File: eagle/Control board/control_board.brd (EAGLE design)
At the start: 100 x 100 mm, 179 parts, among them SW1 SPST_TACT-EVQQ2, SW2 SPST_TACT-EVQQ2, U1 TCA9554A, U2 LM317, U3 LM317, U4 STM32F446, U5 TCA9554A, U6 TCA9554A, X1 JST-XH-02-PIN-LONG-PAD, X10 JST-XH-07-PIN-LONG-PAD, X11 JST-XH-07-PIN-LONG-PAD, X12 JST-XH-02-PIN-LONG-PAD, X13 JST-XH-03-PIN-LONG-PAD, X14 JST-XH-03-PIN-LONG-PAD, X15 JST-XH-08-PIN-LONG-PAD, X16 JST-XH-02-PIN-LONG-PAD, X17 JST-XH-08-PIN-LONG-PAD, X18 JST-XH-02-PIN-LONG-PAD, X2 JST-XH-06-PIN-LONG-PAD, X3 JST-XH-06-PIN-LONG-PAD, X4 JST-XH-06-PIN-LONG-PAD, X5 JST-XH-06-PIN-LONG-PAD, X6 JST-XH-06-PIN-LONG-PAD, X7 JST-XH-06-PIN-LONG-PAD, X8 JST-XH-04-PIN-LONG-PAD, X9 JST-XH-07-PIN-LONG-PAD

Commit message: Nearly done assigning gpio
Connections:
- removed net N$4: SB43.P$1
- removed net N$43: SB42.P$2
- net M1_2: now also SB19.P$1
- net M1_4: now also SB45.P$1
- net M3_1: no longer SB46.P$2
- net M3_3: no longer SB44.P$2
- net RF4_G: now also SB12.P$1; no longer SB1.P$1
- net RF5_G: now also SB13.P$1; no longer SB36.P$2
- net SW1: now also SB50.P$2
- net SW2: now also SB49.P$2
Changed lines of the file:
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@@
 <signal name="RF4_G">
 <contactref element="SB72" pad="P$1"/>
-<contactref element="SB1" pad="P$1"/>
-<wire x1="27.051" y1="36.576" x2="36.195" y2="44.45" width="0" layer="19" extent="1-1"/>
+<contactref element="SB12" pad="P$1"/>
+<wire x1="36.195" y1="44.45" x2="86.995" y2="54.356" width="0" layer="19" extent="1-1"/>
 </signal>
 <signal name="RF5_G">
 <contactref element="SB77" pad="P$1"/>
-<contactref element="SB36" pad="P$2"/>
-<wire x1="27.051" y1="67.056" x2="36.195" y2="55.88" width="0" layer="19" extent="1-1"/>
+<contactref element="SB13" pad="P$1"/>
+<wire x1="36.195" y1="55.88" x2="86.995" y2="56.896" width="0" layer="19" extent="1-1"/>
 </signal>
 <signal name="RF5_X">
@@
 <signal name="M1_4">
 <contactref element="SB88" pad="P$1"/>
+<contactref element="SB45" pad="P$1"/>
+<wire x1="57.15" y1="18.415" x2="66.929" y2="46.736" width="0" layer="19" extent="1-1"/>
 </signal>
 <signal name="M1_1">
@@
 <signal name="M1_2">
 <contactref element="SB86" pad="P$1"/>
+<contactref element="SB19" pad="P$1"/>
+<wire x1="57.15" y1="13.335" x2="86.995" y2="44.196" width="0" layer="19" extent="1-1"/>
 </signal>
 <signal name="M1_3">
@@
 <signal name="M3_1">
 <contactref element="SB90" pad="P$1"/>
-<contactref element="SB46" pad="P$2"/>
 <contactref element="SB7" pad="P$1"/>
-<wire x1="66.929" y1="54.356" x2="86.995" y2="67.056" width="0" layer="19" extent="1-1"/>
 <wire x1="81.28" y1="10.795" x2="66.929" y2="54.356" width="0" layer="19" extent="1-1"/>
 </signal>
@@
 <signal name="M3_3">
 <contactref element="SB92" pad="P$1"/>
-<contactref element="SB44" pad="P$2"/>
 <contactref element="SB8" pad="P$1"/>
-<wire x1="66.929" y1="51.816" x2="86.995" y2="69.596" width="0" layer="19" extent="1-1"/>
 <wire x1="81.28" y1="15.875" x2="66.929" y2="51.816" width="0" layer="19" extent="1-1"/>
 </signal>
@@
 <wire x1="32.385" y1="85.305" x2="32.385" y2="89.535" width="0.3048" layer="1"/>
 <wire x1="34.925" y1="85.305" x2="32.385" y2="85.305" width="0.3048" layer="1"/>
+<contactref element="SB50" pad="P$2"/>
+<wire x1="4.953" y1="26.416" x2="32.385" y2="85.305" width="0" layer="19" extent="1-1"/>
 </signal>
 <signal name="IMU_VCC">
@@
 <contactref element="X8" pad="1"/>
 <wire x1="43.815" y1="73.025" x2="43.815" y2="77.47" width="0.3048" layer="1"/>
-</signal>
-<signal name="N$43">
-<contactref element="SB42" pad="P$2"/>
 </signal>
 <signal name="SW2">
@@
 <wire x1="42.545" y1="89.535" x2="42.545" y2="85.305" width="0.3048" layer="1"/>
 <wire x1="42.545" y1="85.305" x2="45.085" y2="85.305" width="0.3048" layer="1"/>
+<contactref element="SB49" pad="P$2"/>
+<wire x1="4.953" y1="23.876" x2="42.545" y2="85.305" width="0" layer="19" extent="1-1"/>
 </signal>
 <signal name="SERVO2_VCC">
@@
 <contactref element="SB21" pad="P$1"/>
 </signal>
-<signal name="N$4">
-<contactref element="SB43" pad="P$1"/>
-</signal>
 </signals>

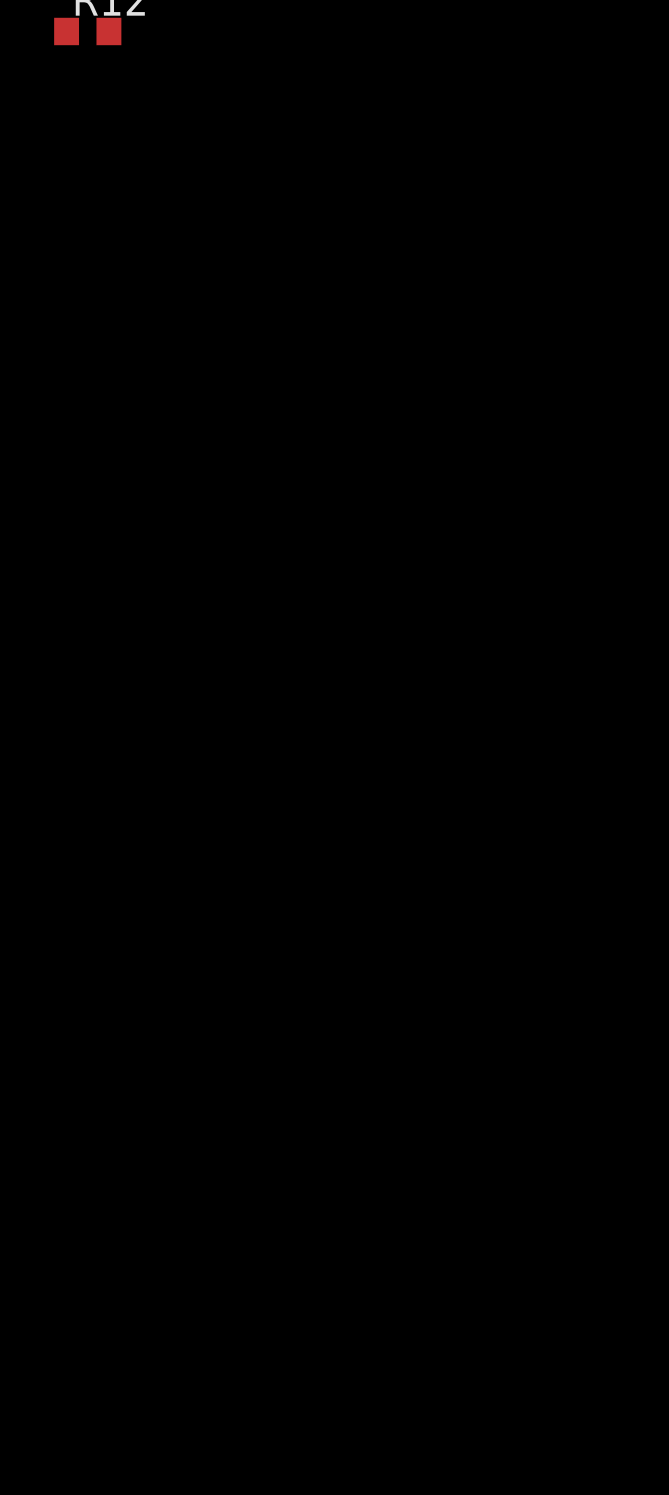
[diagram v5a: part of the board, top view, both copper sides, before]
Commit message: Finished mapping GPIOs. Need to cross check.
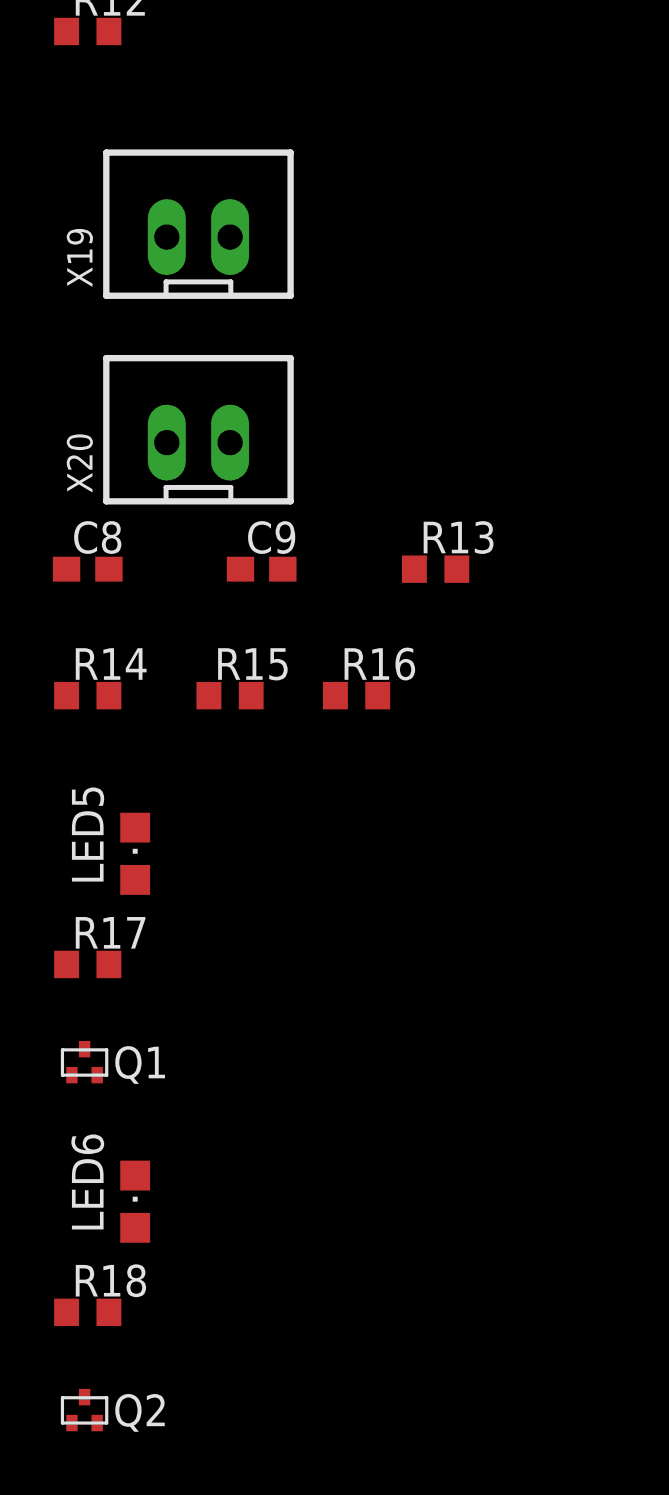
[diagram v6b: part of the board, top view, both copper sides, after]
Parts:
- added C8, C9: 0.1uF, rcl:C0603
- added LED5, LED6: (no value), adafruit:CHIPLED_0805
- added Q1, Q2: RE1C002UN, custom:SOT416FL
- added R13, R14: 4.7k, rcl:R0603
- added R15, R16: 100, rcl:R0603
- added R17, R18: 82, rcl:R0603
- added X19, X20: JST-XH-02-PIN-LONG-PAD, con-jst-xh:JST-XH-02-PACKAGE-LONG-PAD
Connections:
- new net LED_DBG1: Q1.P$1, SB18.P$1
- new net LED_DBG1_A: LED5.A, R17.2
- new net LED_DBG1_K: LED5.C, Q1.P$3
- new net LED_DBG2: Q2.P$1, SB42.P$2
- new net LED_DBG2_A: LED6.A, R18.2
- new net LED_DBG2_K: LED6.C, Q2.P$3
- new net SW3: C8.2, R13.1, SB46.P$2, X19.1
- new net SW3_ILIM: C8.1, R15.2
- new net SW4: C9.2, R14.1, SB47.P$2, X20.1
- new net SW4_ILIM: C9.1, R16.2
- net GND: now also Q1.P$2, Q2.P$2, R15.1, R16.1, X19.2, X20.2
- net PP3V3: now also R13.2, R14.2, R17.1, R18.1
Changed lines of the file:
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@@
 <element name="R11" library="rcl" package="R0603" value="100" x="-33.02" y="-285.75"/>
 <element name="R12" library="rcl" package="R0603" value="100" x="-33.02" y="-290.83"/>
+<element name="X19" library="con-jst-xh" package="JST-XH-02-PACKAGE-LONG-PAD" value="JST-XH-02-PIN-LONG-PAD" x="-28.575" y="-299.085"/>
+<element name="R13" library="rcl" package="R0603" value="4.7k" x="-19.05" y="-312.42"/>
+<element name="C8" library="rcl" package="C0603" value="0.1uF" x="-33.02" y="-312.42"/>
+<element name="X20" library="con-jst-xh" package="JST-XH-02-PACKAGE-LONG-PAD" value="JST-XH-02-PIN-LONG-PAD" x="-28.575" y="-307.34"/>
+<element name="R14" library="rcl" package="R0603" value="4.7k" x="-33.02" y="-317.5"/>
+<element name="C9" library="rcl" package="C0603" value="0.1uF" x="-26.035" y="-312.42"/>
+<element name="R15" library="rcl" package="R0603" value="100" x="-27.305" y="-317.5"/>
+<element name="R16" library="rcl" package="R0603" value="100" x="-22.225" y="-317.5"/>
+<element name="R17" library="rcl" package="R0603" value="82" x="-33.02" y="-328.295"/>
+<element name="LED5" library="adafruit" package="CHIPLED_0805" value="" x="-31.115" y="-323.85"/>
+<element name="Q1" library="custom" package="SOT416FL" value="RE1C002UN" x="-33.655" y="-332.74">
+<attribute name="VALUE" value="RE1C002UN" x="-33.655" y="-332.74" size="1.778" layer="27" display="off"/>
+<attribute name="DIGI" value="RE1C002UNTCLCT-ND" x="-33.655" y="-332.74" size="1.778" layer="27" display="off"/>
+</element>
+<element name="R18" library="rcl" package="R0603" value="82" x="-33.02" y="-342.265"/>
+<element name="LED6" library="adafruit" package="CHIPLED_0805" value="" x="-31.115" y="-337.82"/>
+<element name="Q2" library="custom" package="SOT416FL" value="RE1C002UN" x="-33.655" y="-346.71">
+<attribute name="DIGI" value="RE1C002UNTCLCT-ND" x="-40.005" y="-340.995" size="1.778" layer="27" display="off"/>
+</element>
 </elements>
 <signals>
@@
 <contactref element="R11" pad="1"/>
 <contactref element="R12" pad="1"/>
+<contactref element="X19" pad="2"/>
+<contactref element="R15" pad="1"/>
+<contactref element="X20" pad="2"/>
+<contactref element="R16" pad="1"/>
+<contactref element="Q1" pad="P$2"/>
+<contactref element="Q2" pad="P$2"/>
 <wire x1="-31.75" y1="-215.0999" x2="-33.87" y2="-220.345" width="0" layer="19" extent="1-1"/>
 <wire x1="-30.48" y1="-215.0999" x2="-31.75" y2="-215.0999" width="0" layer="19" extent="1-1"/>
@@
 <wire x1="-33.87" y1="-285.75" x2="-32.61" y2="-275.495" width="0" layer="19" extent="1-1"/>
 <wire x1="-33.87" y1="-290.83" x2="-33.87" y2="-285.75" width="0" layer="19" extent="1-1"/>
+<wire x1="-27.305" y1="-299.085" x2="-33.87" y2="-290.83" width="0" layer="19" extent="1-1"/>
+<wire x1="-27.305" y1="-307.34" x2="-27.305" y2="-299.085" width="0" layer="19" extent="1-1"/>
+<wire x1="-28.155" y1="-317.5" x2="-27.305" y2="-307.34" width="0" layer="19" extent="1-1"/>
+<wire x1="-23.075" y1="-317.5" x2="-28.155" y2="-317.5" width="0" layer="19" extent="1-1"/>
+<wire x1="-32.639" y1="-332.74" x2="-28.155" y2="-317.5" width="0" layer="19" extent="1-1"/>
+<wire x1="-32.639" y1="-346.71" x2="-32.639" y2="-332.74" width="0" layer="19" extent="1-1"/>
 <wire x1="-33.87" y1="-192.405" x2="-31.75" y2="-215.0999" width="0" layer="19" extent="1-1"/>
 <wire x1="-33.02" y1="-187.1599" x2="-33.87" y2="-192.405" width="0" layer="19" extent="1-1"/>
@@
 <contactref element="C7" pad="2"/>
 <contactref element="U6" pad="2"/>
+<contactref element="R13" pad="2"/>
+<contactref element="R14" pad="2"/>
+<contactref element="R17" pad="1"/>
+<contactref element="R18" pad="1"/>
 <wire x1="-33.02" y1="-215.0999" x2="-32.17" y2="-220.345" width="0" layer="19" extent="1-1"/>
 <wire x1="-33.02" y1="-229.4001" x2="-32.17" y2="-220.345" width="0" layer="19" extent="1-1"/>
@@
 <wire x1="-16.09" y1="-187.325" x2="-32.17" y2="-192.405" width="0" layer="19" extent="1-1"/>
 <wire x1="3.175" y1="-121.285" x2="-33.02" y2="-177.3301" width="0" layer="19" extent="1-1"/>
+<wire x1="-18.2" y1="-312.42" x2="-32.17" y2="-244.475" width="0" layer="19" extent="1-1"/>
+<wire x1="-32.17" y1="-317.5" x2="-18.2" y2="-312.42" width="0" layer="19" extent="1-1"/>
+<wire x1="-33.87" y1="-328.295" x2="-32.17" y2="-317.5" width="0" layer="19" extent="1-1"/>
+<wire x1="-33.87" y1="-342.265" x2="-33.87" y2="-328.295" width="0" layer="19" extent="1-1"/>
 <wire x1="46.355" y1="67.31" x2="3.175" y2="-121.285" width="0" layer="19" extent="1-1"/>
 <wire x1="45.085" y1="83.605" x2="46.101" y2="78.74" width="0" layer="19" extent="1-1"/>
@@
 <contactref element="SB21" pad="P$1"/>
 </signal>
+<signal name="SW3">
+<contactref element="R13" pad="1"/>
+<contactref element="X19" pad="1"/>
+<contactref element="C8" pad="2"/>
+<contactref element="SB46" pad="P$2"/>
+<wire x1="-29.845" y1="-299.085" x2="86.995" y2="67.056" width="0" layer="19" extent="1-1"/>
+<wire x1="-32.17" y1="-312.42" x2="-29.845" y2="-299.085" width="0" layer="19" extent="1-1"/>
+<wire x1="-19.9" y1="-312.42" x2="-32.17" y2="-312.42" width="0" layer="19" extent="1-1"/>
+</signal>
+<signal name="SW4">
+<contactref element="R14" pad="1"/>
+<contactref element="X20" pad="1"/>
+<contactref element="C9" pad="2"/>
+<contactref element="SB47" pad="P$2"/>
+<wire x1="-29.845" y1="-307.34" x2="86.995" y2="64.516" width="0" layer="19" extent="1-1"/>
+<wire x1="-25.185" y1="-312.42" x2="-29.845" y2="-307.34" width="0" layer="19" extent="1-1"/>
+<wire x1="-33.87" y1="-317.5" x2="-25.185" y2="-312.42" width="0" layer="19" extent="1-1"/>
+</signal>
+<signal name="SW3_ILIM">
+<contactref element="C8" pad="1"/>
+<contactref element="R15" pad="2"/>
+<wire x1="-26.455" y1="-317.5" x2="-33.87" y2="-312.42" width="0" layer="19" extent="1-1"/>
+</signal>
+<signal name="SW4_ILIM">
+<contactref element="C9" pad="1"/>
+<contactref element="R16" pad="2"/>
+<wire x1="-21.375" y1="-317.5" x2="-26.885" y2="-312.42" width="0" layer="19" extent="1-1"/>
+</signal>
+<signal name="LED_DBG1_K">
+<contactref element="Q1" pad="P$3"/>
+<contactref element="LED5" pad="C"/>
+<wire x1="-31.115" y1="-322.8" x2="-33.147" y2="-331.6986" width="0" layer="19" extent="1-1"/>
+</signal>
+<signal name="LED_DBG1">
+<contactref element="Q1" pad="P$1"/>
+<contactref element="SB18" pad="P$1"/>
+<wire x1="-33.655" y1="-332.74" x2="86.995" y2="41.656" width="0" layer="19" extent="1-1"/>
+</signal>
+<signal name="LED_DBG1_A">
+<contactref element="R17" pad="2"/>
+<contactref element="LED5" pad="A"/>
+<wire x1="-31.115" y1="-324.9" x2="-32.17" y2="-328.295" width="0" layer="19" extent="1-1"/>
+</signal>
+<signal name="LED_DBG2_A">
+<contactref element="R18" pad="2"/>
+<contactref element="LED6" pad="A"/>
+<wire x1="-31.115" y1="-338.87" x2="-32.17" y2="-342.265" width="0" layer="19" extent="1-1"/>
+</signal>
+<signal name="LED_DBG2_K">
+<contactref element="Q2" pad="P$3"/>
+<contactref element="LED6" pad="C"/>
+<wire x1="-31.115" y1="-336.77" x2="-33.147" y2="-345.6686" width="0" layer="19" extent="1-1"/>
+</signal>
+<signal name="LED_DBG2">
+<contactref element="Q2" pad="P$1"/>
+<contactref element="SB42" pad="P$2"/>
+<wire x1="4.953" y1="69.596" x2="-33.655" y2="-346.71" width="0" layer="19" extent="1-1"/>
+</signal>
 </signals>

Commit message: Added configs in Cube.
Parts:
- added R19, R20, R21, R22: 3.3k, rcl:R0603
- C1, C2: value 0.1u -> 0.1uF
- LED1, LED2, LED3, LED4, LED5, LED6: value (none) -> GREEN
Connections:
- new net N$10: U4.P$76
- new net N$11: U4.P$46
- new net N$12: U4.P$6
- new net N$13: U4.P$45
- new net N$14: U4.P$70
- new net N$15: U4.P$12
- new net N$16: U4.P$33
- new net N$17: U4.P$5
- new net N$18: U4.P$18
- new net N$19: U4.P$16
- new net N$2: U4.P$9
- new net N$20: SB1.P$1
- new net N$21: SB2.P$1
- new net N$22: SB3.P$1
- new net N$23: SB4.P$1
- new net N$24: SB5.P$1
- new net N$25: SB6.P$1
- new net N$26: SB10.P$1
- new net N$27: SB14.P$1
- new net N$28: SB15.P$1
- new net N$29: SB16.P$1
- new net N$30: SB20.P$1
- new net N$31: SB28.P$1
- new net N$32: SB35.P$2
- new net N$33: SB34.P$2
- new net N$34: SB33.P$2
- new net N$35: SB36.P$2
- new net N$36: SB37.P$2
- new net N$37: SB38.P$2
- new net N$38: SB43.P$1
- new net N$39: SB44.P$2
- new net N$4: U4.P$10
- new net N$40: U1.13
- new net N$41: U5.13
- new net N$42: U6.13
- new net N$5: U4.P$11
- new net N$6: U4.P$26
- new net N$7: U4.P$48
- new net N$8: U4.P$56
- new net N$9: U4.P$74
- net I2C2_SCL: now also R21.2; no longer SB116.P$1, SB118.P$1, SB120.P$1, SB70.P$1, SB75.P$1, SB80.P$1
- net I2C2_SDA: now also R22.2; no longer SB107.P$1, SB117.P$1, SB119.P$1, SB71.P$1, SB76.P$1, SB81.P$1
- net I2C3_SCL: now also R19.2, SB116.P$1, SB118.P$1, SB120.P$1, SB70.P$1, SB75.P$1, SB80.P$1
- net I2C3_SDA: now also R20.2, SB107.P$1, SB117.P$1, SB119.P$1, SB71.P$1, SB76.P$1, SB81.P$1
- net PP3V3: now also R19.1, R20.1, R21.1, R22.1
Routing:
- net I2C2_SDA: track 77.0 -> 73.9 mm
- net I2C2_SCL: track 77.0 -> 73.9 mm

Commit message: Almost done routing
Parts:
- removed SB74, SB79, SB84, SB85, SB86, SB87, SB88, SB89, SB90, SB91, SB92, SB93, SB95, SB97: SOLDER_BRIDGE, custom:SOLDER_BRIDGE
- removed U3: LM317, custom:317TS
- added C10, C11: 22uF, rcl:C0603
- added U7: AZ1085CD, custom:TO252
- C1, C2: value 0.1uF -> 10uF
- R1: value (none) -> 178
- R17, R8: value 82 -> 430
- R2: value (none) -> 287
- R3: value (none) -> 100
- R4: value (none) -> 301
- R7: value 430 -> 82
- U2: value LM317 -> AZ1085CD; device custom:317TS -> custom:TO252
- moved R21 448.6 mm to (37.6, 82.3), turned to 90 degrees
- moved R22 439.8 mm to (42.8, 67.4), turned to 90 degrees
- moved Q2 422.9 mm to (16.6, 73.2), turned to 90 degrees
- moved R14 422.5 mm to (65.0, 93.5), turned to 90 degrees
- moved R18 420.5 mm to (13.1, 75.7), turned to 180 degrees
- moved R20 419.1 mm to (64.0, 52.1), turned to 270 degrees
- moved R16 417.6 mm to (67.2, 90.4), turned to 270 degrees
- moved R15 415.7 mm to (52.7, 90.4), turned to 270 degrees
- moved R19 414.6 mm to (66.2, 52.1), turned to 270 degrees
- moved LED6 413.8 mm to (13.1, 73.7), turned to 270 degrees
- moved C9 413.0 mm to (65.0, 90.4), turned to 90 degrees
- moved R13 411.8 mm to (50.5, 93.5), turned to 90 degrees
- moved C8 411.4 mm to (50.5, 90.4), turned to 90 degrees
- moved X20 409.4 mm to (59.6, 92.5), turned to 180 degrees
- moved X19 398.4 mm to (45.1, 92.5), turned to 180 degrees
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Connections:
- net PP8V_CONN renamed PP7V_CONN
- removed net MOTOR1_1EN: SB85.P$2, X9.4
- removed net MOTOR1_2EN: SB86.P$2, X9.5
- removed net MOTOR1_3EN: SB87.P$2, X9.6
- removed net MOTOR1_4EN: SB88.P$2, X9.7
- removed net MOTOR2_1EN: SB74.P$2, X10.4
- removed net MOTOR2_2EN: SB79.P$2, X10.5
- removed net MOTOR2_3EN: SB84.P$2, X10.6
- removed net MOTOR2_4EN: SB89.P$2, X10.7
- removed net MOTOR3_1EN: SB90.P$2, X11.4
- removed net MOTOR3_2EN: SB91.P$2, X11.5
- removed net MOTOR3_3EN: SB92.P$2, X11.6
- removed net MOTOR3_4EN: SB93.P$2, X11.7
- removed net SERVO1_PWM: SB95.P$2, X13.2
- removed net SERVO2_PWM: SB97.P$2, X14.2
- net GND: now also C10.2, C11.2
- net I2C2_SCL: now also SB120.P$1, SB70.P$1, SB75.P$1, SB80.P$1; no longer SB55.P$1, SB60.P$1, SB65.P$1
- net I2C2_SDA: now also SB119.P$1, SB71.P$1, SB76.P$1, SB81.P$1; no longer SB56.P$1, SB61.P$1, SB66.P$1
- net I2C3_SCL: now also SB55.P$1, SB60.P$1, SB65.P$1; no longer SB120.P$1, SB70.P$1, SB75.P$1, SB80.P$1
- net I2C3_SDA: now also SB56.P$1, SB61.P$1, SB66.P$1; no longer SB119.P$1, SB71.P$1, SB76.P$1, SB81.P$1
- net LED_3V3: now also LED1.A, R7.2; no longer LED2.A, R8.2
- net LED_5V: now also LED2.A, R8.2; no longer LED1.A, R7.2
- net M1_1: now also X9.4; no longer SB85.P$1
- net M1_2: now also X9.5; no longer SB86.P$1
- net M1_3: now also X9.6; no longer SB87.P$1
- net M1_4: now also X9.7; no longer SB88.P$1
- net M2_1: now also X10.4; no longer SB74.P$1
- net M2_2: now also X10.5; no longer SB79.P$1
- net M2_3: now also X10.6; no longer SB84.P$1
- net M2_4: now also X10.7; no longer SB89.P$1
- net M3_1: now also X11.4; no longer SB90.P$1
- net M3_2: now also X11.5; no longer SB91.P$1
- net M3_3: now also X11.6; no longer SB92.P$1
- net M3_4: now also X11.7; no longer SB93.P$1
- net N$1: now also U2.1; no longer U3.1
- net N$3: now also U7.1; no longer U2.1
- net PP3V3: now also C10.1, R1.1, R7.1, U7.2; no longer R17.1, R3.1, R8.1, U3.2
- net PP5V: now also C11.1, R17.1, R3.1, R8.1; no longer R1.1, R7.1
- net PP7V: now also U7.3; no longer U3.3
- net SERVO1: now also X13.2; no longer SB95.P$1
- net SERVO2: now also X14.2; no longer SB97.P$1
- net SW2: now also SB47.P$2; no longer SB49.P$2
- net SW3: now also SB49.P$2; no longer SB46.P$2
- net SW4: now also SB46.P$2; no longer SB47.P$2
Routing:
- net PP3V3: track 13.8 -> 141.9 mm, vias 0 -> 4
- net SW3: track 0.00 -> 117.2 mm, vias 0 -> 3
- net I2C3_SCL: track 0.00 -> 110.4 mm, vias 0 -> 4
- net I2C3_SDA: track 0.00 -> 107.9 mm, vias 0 -> 4
- net SW1: track 6.77 -> 112.7 mm, vias 0 -> 3
- net M1_3: track 0.00 -> 92.6 mm, vias 0 -> 2
- net PP5V: track 24.1 -> 113.6 mm
- net M2_1: track 0.00 -> 76.9 mm, vias 0 -> 1
- net RF1_X: track 0.00 -> 72.4 mm
- net RF4_G: track 0.00 -> 64.2 mm, vias 0 -> 1
- net M2_3: track 0.00 -> 62.6 mm, vias 0 -> 1
- net M3_1: track 0.00 -> 62.1 mm, vias 0 -> 1
- net RF2_X: track 0.00 -> 60.7 mm
- net PPBATT: track 0.00 -> 56.7 mm
- net RF5_G: track 0.00 -> 56.4 mm, vias 0 -> 1
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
